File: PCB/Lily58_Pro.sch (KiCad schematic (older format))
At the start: 83 parts, among them J1 LED, J2 4PIN, J3 OLED, P1 i2c_pin, P2 i2c_pin, SW1 SW_PUSH, SW10 SW_PUSH, SW11 SW_PUSH, SW12 SW_PUSH, SW13 SW_PUSH, SW14 SW_PUSH, SW15 SW_PUSH, SW16 SW_PUSH, SW17 SW_PUSH, SW18 SW_PUSH, SW19 SW_PUSH, SW2 SW_PUSH, SW20 SW_PUSH, SW21 SW_PUSH, SW22 SW_PUSH, SW23 SW_PUSH, SW24 SW_PUSH, SW25 Rotary_Encoder_Switch, SW26 SW_PUSH, SW27 SW_PUSH, SW28 SW_PUSH, SW29 SW_PUSH, SW3 SW_PUSH, SW4 SW_PUSH, SW5 SW_PUSH, SW6 SW_PUSH, SW7 SW_PUSH, SW8 SW_PUSH, SW9 SW_PUSH, U1 ProMicro

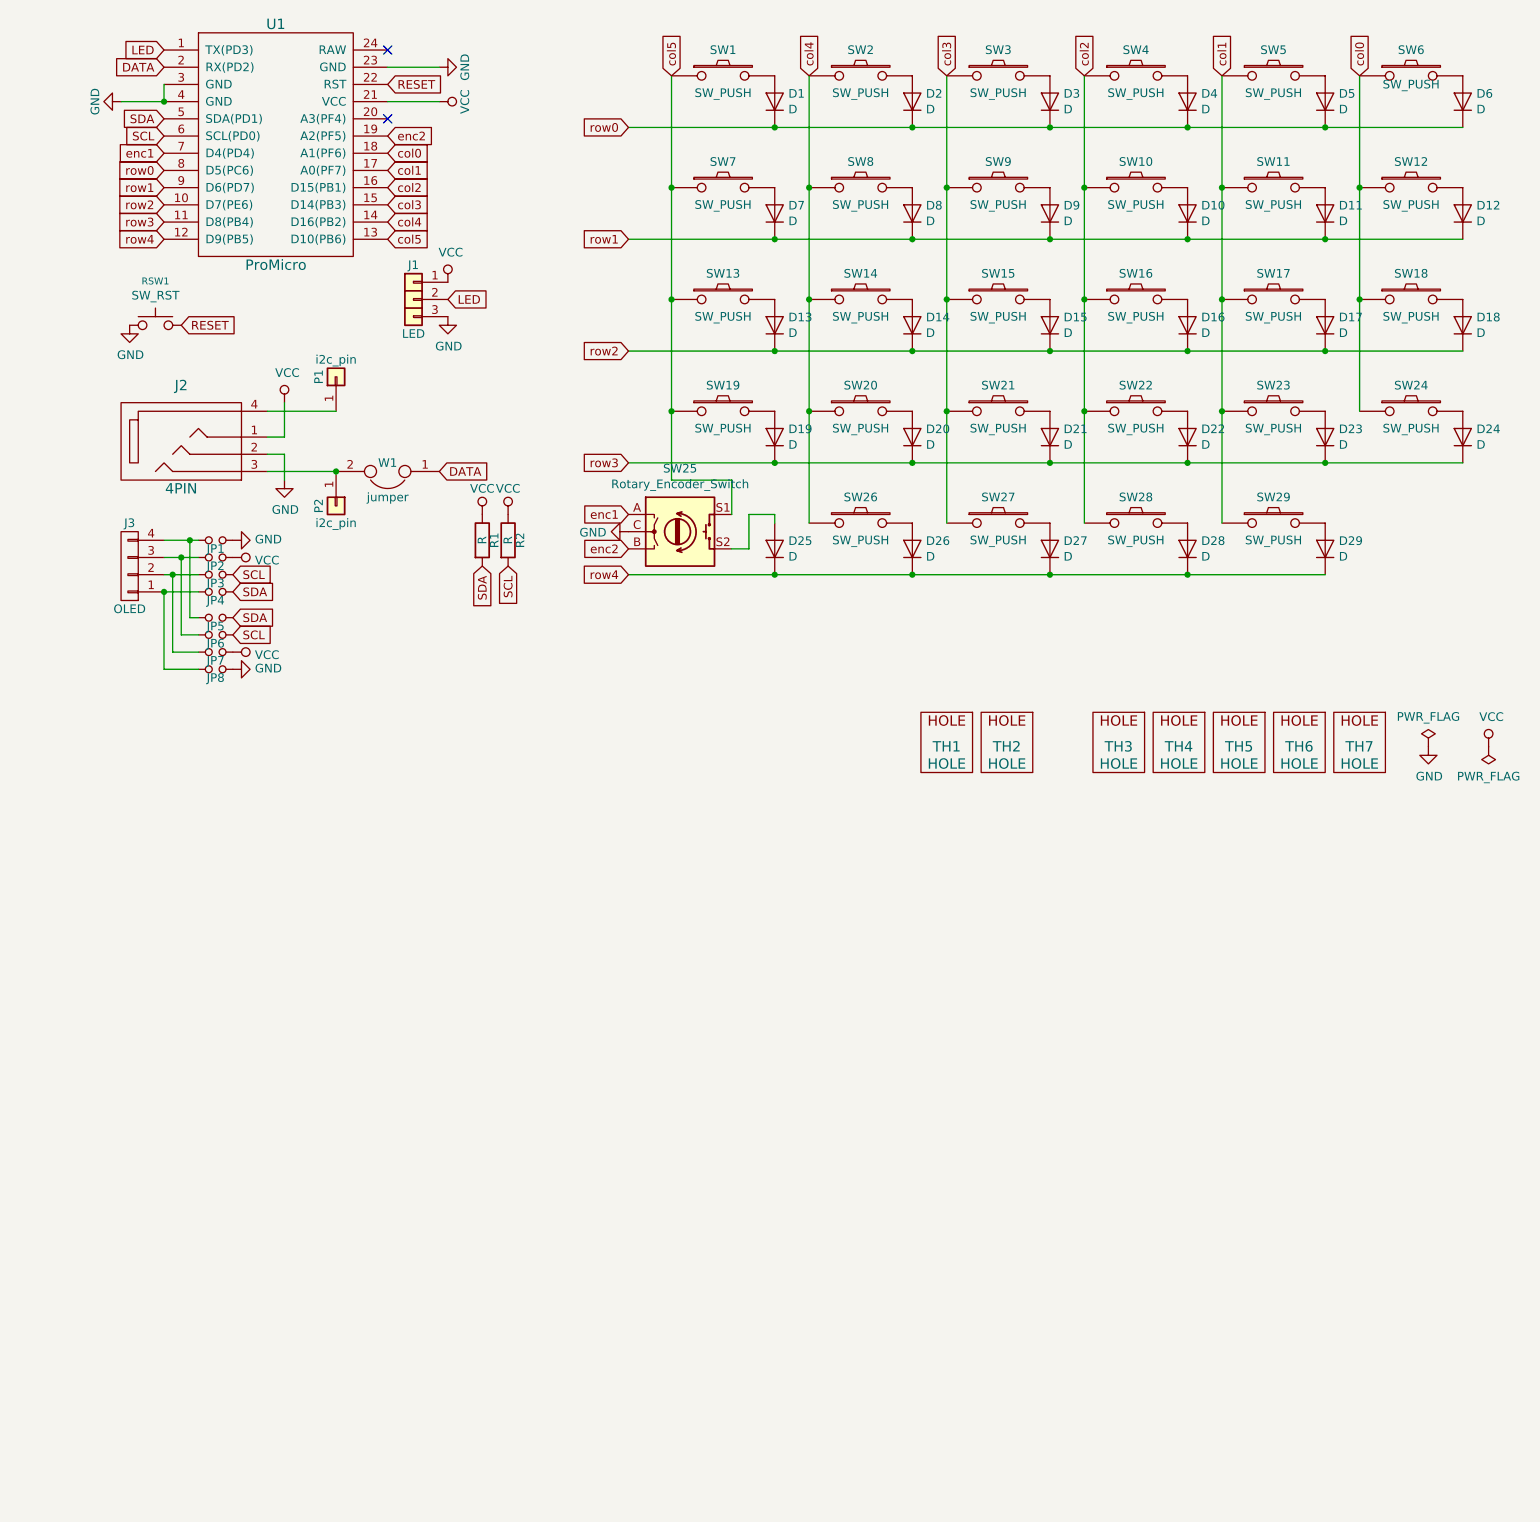
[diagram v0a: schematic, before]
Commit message: Update schematics with rgb backlight/underglow
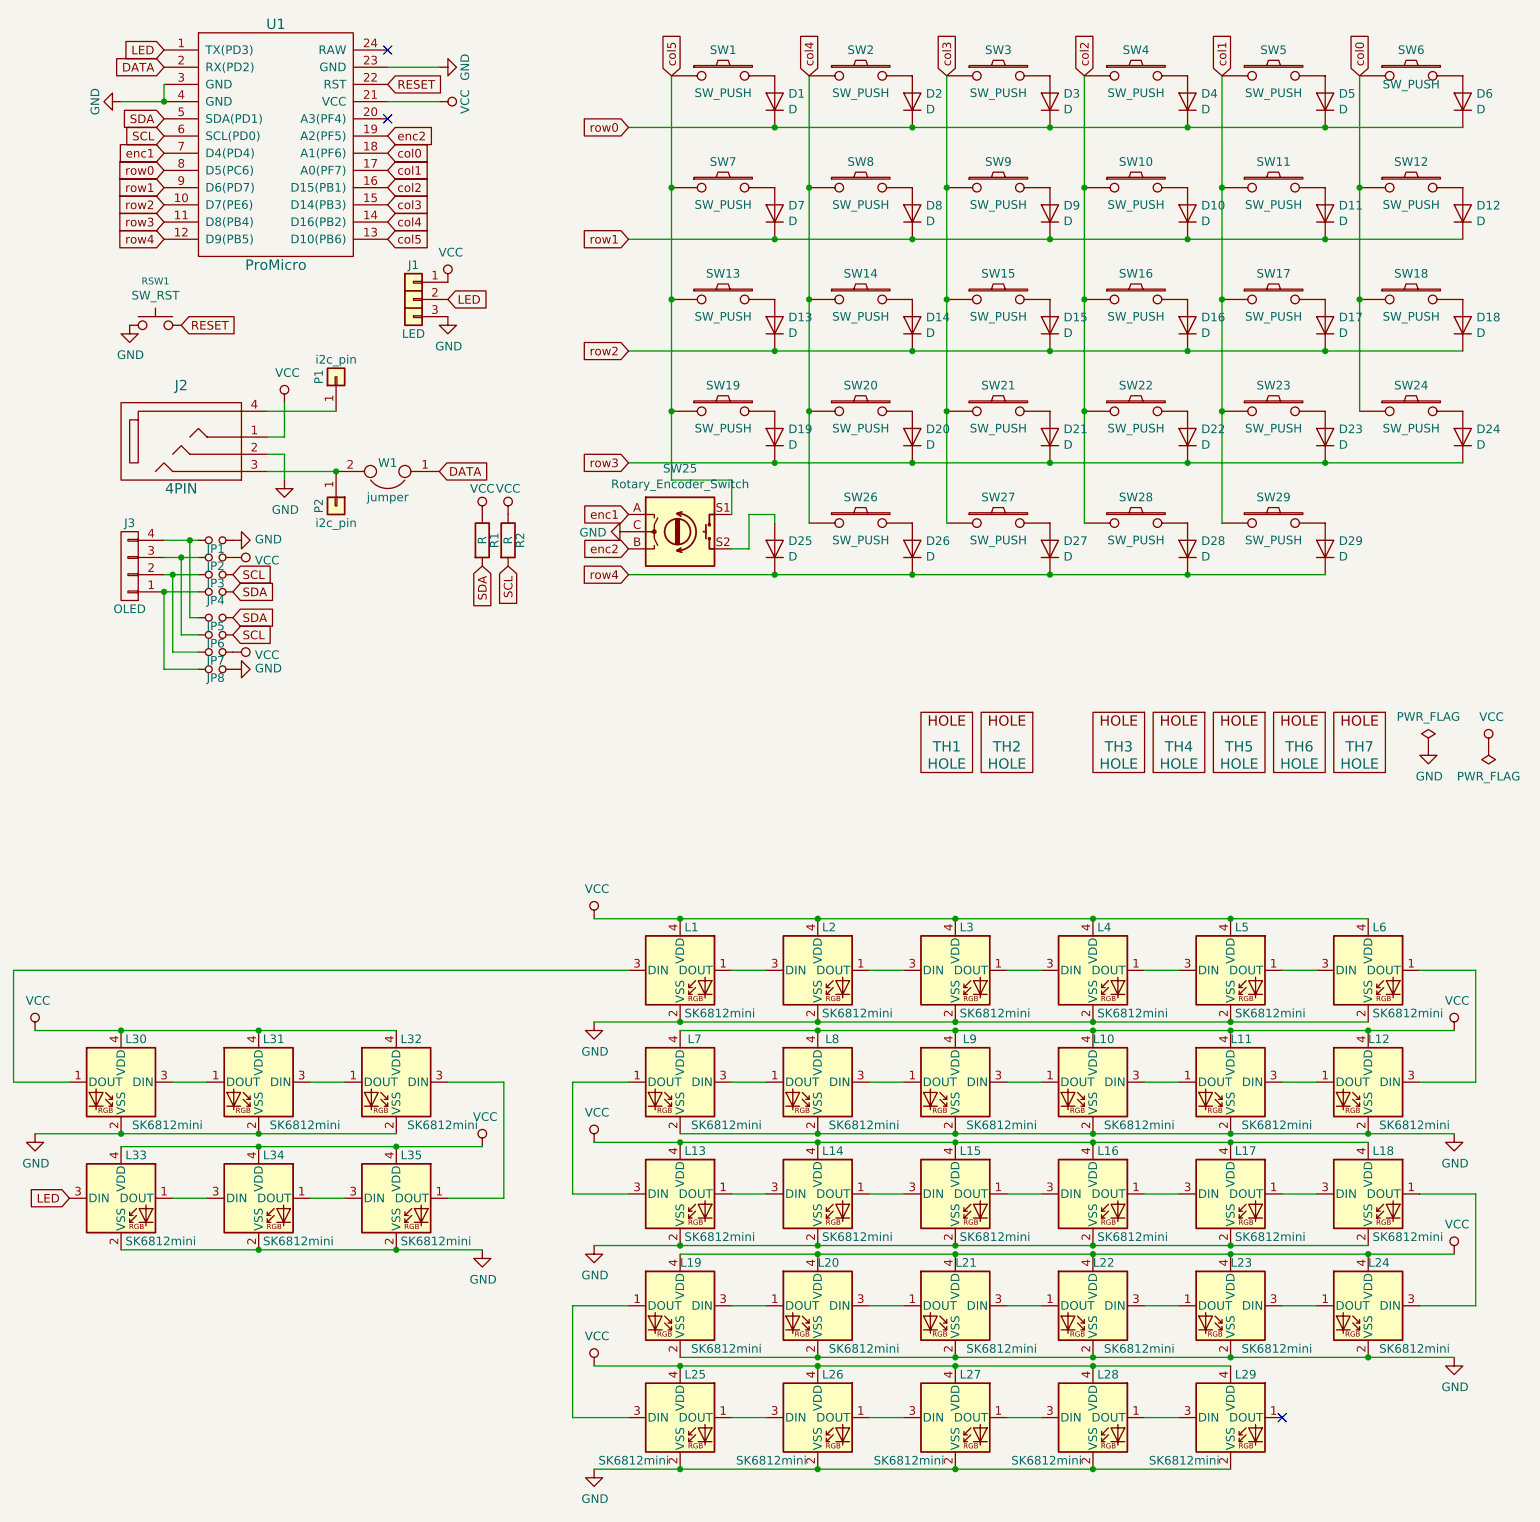
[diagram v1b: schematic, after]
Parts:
- added L1, L10, L11, L12, L13, L14, L15, L16, L17, L18, L19, L2, L20, L21, L22, L23, L24, L25, L26, L27, L28, L29, L3, L4, L5, L6, L7, L8, L9: SK6812mini, fractory:SK6812MINI, symbol LED:SK6812MINI
- added L30, L31, L32, L34, L35: SK6812mini, fractory:SK6812MINI_underglow, symbol LED:SK6812MINI
- added L33: SK6812mini, Lily58-footprint:SK6812MINI_underglow_rev, symbol LED:SK6812MINI
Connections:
- net GND: now also L1.2 (VSS), L10.2 (VSS), L11.2 (VSS), L12.2 (VSS), L13.2 (VSS), L14.2 (VSS), L15.2 (VSS), L16.2 (VSS), L17.2 (VSS), L18.2 (VSS), L19.2 (VSS), L2.2 (VSS), L20.2 (VSS), L21.2 (VSS), L22.2 (VSS), L23.2 (VSS), L24.2 (VSS), L25.2 (VSS), L26.2 (VSS), L27.2 (VSS), L28.2 (VSS), L29.2 (VSS), L3.2 (VSS), L30.2 (VSS), L31.2 (VSS), L32.2 (VSS), L33.2 (VSS), L34.2 (VSS), L35.2 (VSS), L4.2 (VSS), L5.2 (VSS), L6.2 (VSS), L7.2 (VSS), L8.2 (VSS), L9.2 (VSS)
- net LED: now also L33.3 (DIN)
- net VCC: now also L1.4 (VDD), L10.4 (VDD), L11.4 (VDD), L12.4 (VDD), L13.4 (VDD), L14.4 (VDD), L15.4 (VDD), L16.4 (VDD), L17.4 (VDD), L18.4 (VDD), L19.4 (VDD), L2.4 (VDD), L20.4 (VDD), L21.4 (VDD), L22.4 (VDD), L23.4 (VDD), L24.4 (VDD), L25.4 (VDD), L26.4 (VDD), L27.4 (VDD), L28.4 (VDD), L29.4 (VDD), L3.4 (VDD), L30.4 (VDD), L31.4 (VDD), L32.4 (VDD), L33.4 (VDD), L34.4 (VDD), L35.4 (VDD), L4.4 (VDD), L5.4 (VDD), L6.4 (VDD), L7.4 (VDD), L8.4 (VDD), L9.4 (VDD)
- new net: L28.1 (DOUT), L29.3 (DIN)
- new net: L27.1 (DOUT), L28.3 (DIN)
- new net: L26.1 (DOUT), L27.3 (DIN)
- new net: L25.1 (DOUT), L26.3 (DIN)
- new net: L19.1 (DOUT), L25.3 (DIN)
- new net: L23.3 (DIN), L24.1 (DOUT)
- new net: L18.1 (DOUT), L24.3 (DIN)
- new net: L22.3 (DIN), L23.1 (DOUT)
- new net: L21.3 (DIN), L22.1 (DOUT)
- new net: L20.3 (DIN), L21.1 (DOUT)
- new net: L19.3 (DIN), L20.1 (DOUT)
- new net: L17.1 (DOUT), L18.3 (DIN)
- new net: L16.1 (DOUT), L17.3 (DIN)
- new net: L15.1 (DOUT), L16.3 (DIN)
- new net: L14.1 (DOUT), L15.3 (DIN)
- new net: L13.1 (DOUT), L14.3 (DIN)
- new net: L13.3 (DIN), L7.1 (DOUT)
- new net: L11.3 (DIN), L12.1 (DOUT)
- new net: L12.3 (DIN), L6.1 (DOUT)
- new net: L10.3 (DIN), L11.1 (DOUT)
- new net: L10.1 (DOUT), L9.3 (DIN)
- new net: L8.3 (DIN), L9.1 (DOUT)
- new net: L7.3 (DIN), L8.1 (DOUT)
- new net: L5.1 (DOUT), L6.3 (DIN)
- new net: L4.1 (DOUT), L5.3 (DIN)
- new net: L3.1 (DOUT), L4.3 (DIN)
- new net: L2.1 (DOUT), L3.3 (DIN)
- new net: L1.1 (DOUT), L2.3 (DIN)
- new net: L1.3 (DIN), L30.1 (DOUT)
- new net: L30.3 (DIN), L31.1 (DOUT)
- new net: L31.3 (DIN), L32.1 (DOUT)
- new net: L32.3 (DIN), L35.1 (DOUT)
- new net: L34.1 (DOUT), L35.3 (DIN)
- new net: L33.1 (DOUT), L34.3 (DIN)
- no-connect marks 2 -> 3

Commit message: WIP underglow/backlight
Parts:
- removed L25: SK6812mini, fractory:SK6812MINI, symbol LED:SK6812MINI
- L33: footprint Lily58-footprint:SK6812MINI_underglow_rev -> fractory:SK6812MINI_underglow
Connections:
- net at L26.3 (DIN): now also L19.1 (DOUT)
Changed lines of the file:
@@
 Wire Wire Line
 	5250 8100 4925 8100
-Connection ~ 5550 10350
-Wire Wire Line
-	5050 10350 5550 10350
 Connection ~ 5550 9050
 Wire Wire Line
@@
 	1    0    0    -1
 $EndComp
-Wire Wire Line
-	6350 10350 5550 10350
-Wire Wire Line
-	5850 10050 6050 10050
 $Comp
 L LED:SK6812MINI L26
@@
 $EndComp
 $Comp
-L power:GND #PWR?
+L power:GND #PWR0104
 U 1 1 5F0746C6
 P 5050 10350
-F 0 "#PWR?" H 5050 10100 50  0001 C CNN
+F 0 "#PWR0104" H 5050 10100 50  0001 C CNN
 F 1 "GND" H 5055 10177 50  0000 C CNN
 F 2 "" H 5050 10350 50  0001 C CNN
@@
 $EndComp
 $Comp
-L power:VCC #PWR?
+L power:VCC #PWR0105
 U 1 1 5F0746CC
 P 5050 9750
-F 0 "#PWR?" H 5050 9600 50  0001 C CNN
+F 0 "#PWR0105" H 5050 9600 50  0001 C CNN
 F 1 "VCC" H 5067 9923 50  0000 C CNN
 F 2 "" H 5050 9750 50  0001 C CNN
 F 3 "" H 5050 9750 50  0001 C CNN
 	1    5050 9750
-	1    0    0    -1
-$EndComp
-$Comp
-L LED:SK6812MINI L25
-U 1 1 5F0746D2
-P 5550 10050
-F 0 "L25" H 5575 10300 50  0000 L CNN
-F 1 "SK6812mini" H 5075 9800 50  0000 L CNN
-F 2 "fractory:SK6812MINI" H 5600 9750 50  0001 L TNN
-F 3 "https://cdn-shop.adafruit.com/product-files/2686/SK6812MINI_REV.01-1-2.pdf" H 5650 9675 50  0001 L TNN
-	1    5550 10050
 	1    0    0    -1
 $EndComp
@@
 $EndComp
 $Comp
-L power:GND #PWR?
+L power:GND #PWR0106
 U 1 1 5F074711
 P 10050 9700
-F 0 "#PWR?" H 10050 9450 50  0001 C CNN
+F 0 "#PWR0106" H 10050 9450 50  0001 C CNN
 F 1 "GND" H 10055 9527 50  0000 C CNN
 F 2 "" H 10050 9700 50  0001 C CNN
@@
 $EndComp
 $Comp
-L power:VCC #PWR?
+L power:VCC #PWR0107
 U 1 1 5F074717
 P 10050 9100
-F 0 "#PWR?" H 10050 8950 50  0001 C CNN
+F 0 "#PWR0107" H 10050 8950 50  0001 C CNN
 F 1 "VCC" H 10067 9273 50  0000 C CNN
 F 2 "" H 10050 9100 50  0001 C CNN
@@
 $EndComp
 $Comp
-L power:GND #PWR?
+L power:GND #PWR0108
 U 1 1 5F074758
 P 5050 9050
-F 0 "#PWR?" H 5050 8800 50  0001 C CNN
+F 0 "#PWR0108" H 5050 8800 50  0001 C CNN
 F 1 "GND" H 5055 8877 50  0000 C CNN
 F 2 "" H 5050 9050 50  0001 C CNN
@@
 $EndComp
 $Comp
-L power:VCC #PWR?
+L power:VCC #PWR0109
 U 1 1 5F07475E
 P 5050 8450
-F 0 "#PWR?" H 5050 8300 50  0001 C CNN
+F 0 "#PWR0109" H 5050 8300 50  0001 C CNN
 F 1 "VCC" H 5067 8623 50  0000 C CNN
 F 2 "" H 5050 8450 50  0001 C CNN
@@
 $EndComp
 $Comp
-L power:GND #PWR?
+L power:GND #PWR0110
 U 1 1 5F0747A3
 P 10050 8400
-F 0 "#PWR?" H 10050 8150 50  0001 C CNN
+F 0 "#PWR0110" H 10050 8150 50  0001 C CNN
 F 1 "GND" H 10055 8227 50  0000 C CNN
 F 2 "" H 10050 8400 50  0001 C CNN
@@
 $EndComp
 $Comp
-L power:VCC #PWR?
+L power:VCC #PWR0111
 U 1 1 5F0747A9
 P 10050 7800
-F 0 "#PWR?" H 10050 7650 50  0001 C CNN
+F 0 "#PWR0111" H 10050 7650 50  0001 C CNN
 F 1 "VCC" H 10067 7973 50  0000 C CNN
 F 2 "" H 10050 7800 50  0001 C CNN
@@
 $EndComp
 $Comp
-L power:GND #PWR?
+L power:GND #PWR0112
 U 1 1 5F0747EA
 P 5050 7750
-F 0 "#PWR?" H 5050 7500 50  0001 C CNN
+F 0 "#PWR0112" H 5050 7500 50  0001 C CNN
 F 1 "GND" H 5055 7577 50  0000 C CNN
 F 2 "" H 5050 7750 50  0001 C CNN
@@
 $EndComp
 $Comp
-L power:VCC #PWR?
+L power:VCC #PWR0113
 U 1 1 5F0747F0
 P 5050 7150
-F 0 "#PWR?" H 5050 7000 50  0001 C CNN
+F 0 "#PWR0113" H 5050 7000 50  0001 C CNN
 F 1 "VCC" H 5067 7323 50  0000 C CNN
 F 2 "" H 5050 7150 50  0001 C CNN
@@
 	7950 10350 8750 10350
 Connection ~ 7950 10350
-Wire Wire Line
-	5050 9750 5550 9750
-Connection ~ 5550 9750
-Wire Wire Line
-	5550 9750 6350 9750
 Connection ~ 6350 9750
 Wire Wire Line
@@
 	7950 9750 8750 9750
 Wire Wire Line
-	4925 10050 5250 10050
-Wire Wire Line
 	1800 7800 2300 7800
 $Comp
-L power:VCC #PWR?
+L power:VCC #PWR0114
 U 1 1 5F074810
 P 1800 7800
-F 0 "#PWR?" H 1800 7650 50  0001 C CNN
+F 0 "#PWR0114" H 1800 7650 50  0001 C CNN
 F 1 "VCC" H 1817 7973 50  0000 C CNN
 F 2 "" H 1800 7800 50  0001 C CNN
@@
 	1800 8400 2300 8400
 $Comp
-L power:GND #PWR?
+L power:GND #PWR0115
 U 1 1 5F074840
 P 1800 8400
-F 0 "#PWR?" H 1800 8150 50  0001 C CNN
+F 0 "#PWR0115" H 1800 8150 50  0001 C CNN
 F 1 "GND" H 1805 8227 50  0000 C CNN
 F 2 "" H 1800 8400 50  0001 C CNN
@@
 	3900 9075 4400 9075
 $Comp
-L power:GND #PWR?
+L power:GND #PWR0116
 U 1 1 5F074847
 P 4400 9075
-F 0 "#PWR?" H 4400 8825 50  0001 C CNN
+F 0 "#PWR0116" H 4400 8825 50  0001 C CNN
 F 1 "GND" H 4405 8902 50  0000 C CNN
 F 2 "" H 4400 9075 50  0001 C CNN
@@
 	3100 8400 3900 8400
 $Comp
-L power:VCC #PWR?
+L power:VCC #PWR0117
 U 1 1 5F074851
 P 4400 8475
-F 0 "#PWR?" H 4400 8325 50  0001 C CNN
+F 0 "#PWR0117" H 4400 8325 50  0001 C CNN
 F 1 "VCC" H 4417 8648 50  0000 C CNN
 F 2 "" H 4400 8475 50  0001 C CNN
@@
 F 0 "L33" H 2325 9025 50  0000 L CNN
 F 1 "SK6812mini" H 2325 8525 50  0000 L CNN
-F 2 "Lily58-footprint:SK6812MINI_underglow_rev" H 2350 8475 50  0001 L TNN
+F 2 "fractory:SK6812MINI_underglow" H 2350 8475 50  0001 L TNN
 F 3 "https://cdn-shop.adafruit.com/product-files/2686/SK6812MINI_REV.01-1-2.pdf" H 2400 8400 50  0001 L TNN
 	1    2300 8775
@@
 Wire Wire Line
 	1675 7450 5250 7450
+Wire Wire Line
+	5050 10350 6350 10350
+Wire Wire Line
+	5050 9750 6350 9750
+Wire Wire Line
+	4925 10050 6050 10050
 $EndSCHEMATC

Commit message: WIP underglow/backlight
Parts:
- added L25: SK6812mini, fractory:SK6812MINI, symbol LED:SK6812MINI
- W1: footprint Lily58-footprint:jumper_data -> fractory:SolderJumper-2_P1.3mm_Bridged_Pad1.0x1.5mm
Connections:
- net GND: now also L25.2 (VSS)
- net VCC: now also L25.4 (VDD)
- net at L26.3 (DIN): now also L25.1 (DOUT); no longer L19.1 (DOUT)
- new net: L19.1 (DOUT), L25.3 (DIN)

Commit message: Finishing underglow/backlight
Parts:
- SW25: footprint fractory:RotaryEncoder_Alps_EC11E-Switch_Vertical_H20mm -> fractory:RotaryEncoder_optional
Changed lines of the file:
@@
 F 0 "SW25" H 5550 5267 50  0000 C CNN
 F 1 "Rotary_Encoder_Switch" H 5550 5176 50  0000 C CNN
-F 2 "fractory:RotaryEncoder_Alps_EC11E-Switch_Vertical_H20mm" H 5400 5060 50  0001 C CNN
+F 2 "fractory:RotaryEncoder_optional" H 5400 5060 50  0001 C CNN
 F 3 "~" H 5550 5160 50  0001 C CNN
 	1    5550 4900

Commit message: WIP net
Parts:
- renumbered SW25 to SW
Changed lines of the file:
@@
 Wire Wire Line
 	5850 4600 5500 4600
-$Comp
-L Device:Rotary_Encoder_Switch SW25
-U 1 1 5F03D82E
-P 5550 4900
-F 0 "SW25" H 5550 5267 50  0000 C CNN
-F 1 "Rotary_Encoder_Switch" H 5550 5176 50  0000 C CNN
-F 2 "fractory:RotaryEncoder_optional" H 5400 5060 50  0001 C CNN
-F 3 "~" H 5550 5160 50  0001 C CNN
-	1    5550 4900
-	1    0    0    -1
-$EndComp
 Text GLabel 2550 2700 0    50   Input ~ 0
 enc1
@@
 	-1   0    0    1
 $EndComp
+$Comp
+L Device:Rotary_Encoder_Switch SW
+U 1 1 5F03D82E
+P 5550 4900
+F 0 "SW" H 5550 5267 50  0000 C CNN
+F 1 "Rotary_Encoder_Switch" H 5550 5176 50  0000 C CNN
+F 2 "fractory:RotaryEncoder_optional" H 5400 5060 50  0001 C CNN
+F 3 "~" H 5550 5160 50  0001 C CNN
+	1    5550 4900
+	1    0    0    -1
+$EndComp
 $EndSCHEMATC
